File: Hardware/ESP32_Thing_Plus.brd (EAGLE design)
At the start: 22.9 x 58.4 mm, 106 parts, among them J3 QWIIC_RIGHT_ANGLE, J6 microSD, Q2 MBT3904DW1T1, Q3 20V/4.2A/52mΩ/1.4W, U1 MCP73831, U2 ESP-WROOM-32NARROW, U3 AP2112K-3.3, U4 MAX17048, U5 AP2112K-3.3, U6 THINGPLUS_LOGICAL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

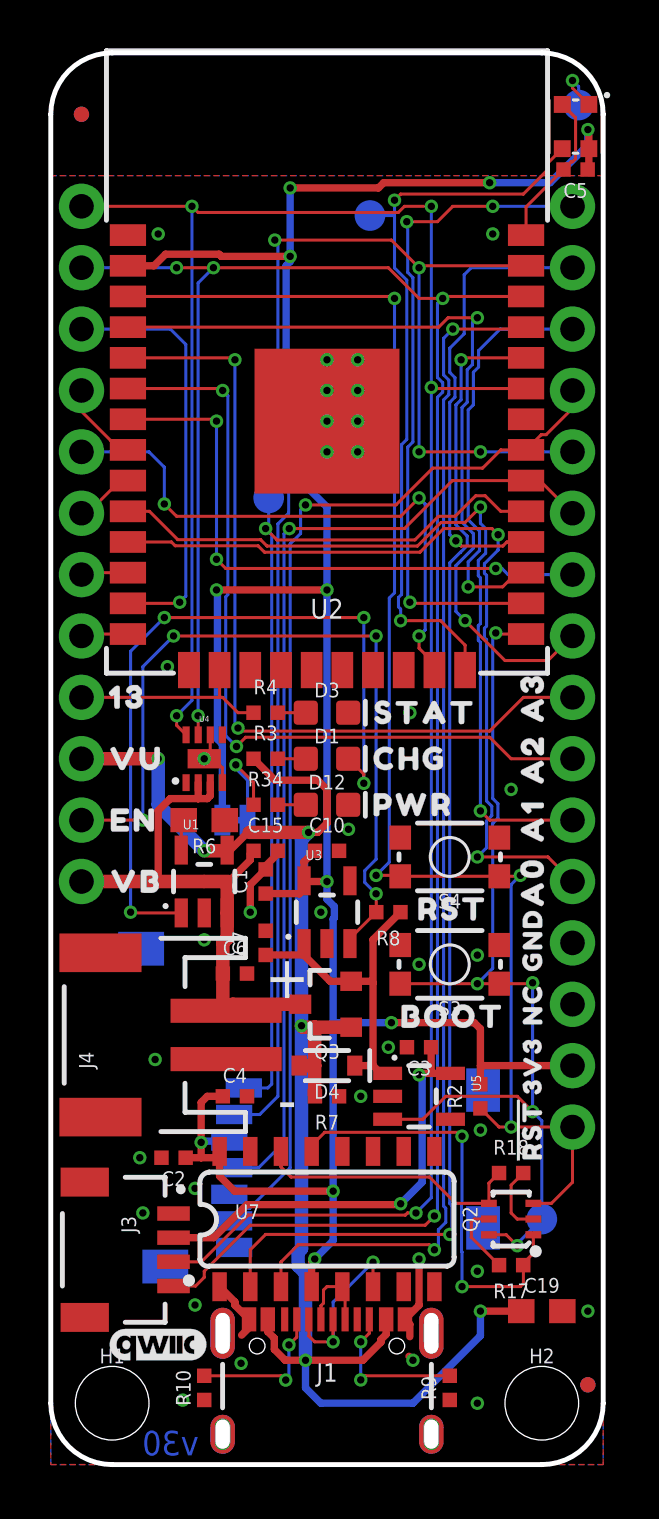
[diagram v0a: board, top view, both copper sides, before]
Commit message: Add test sketches
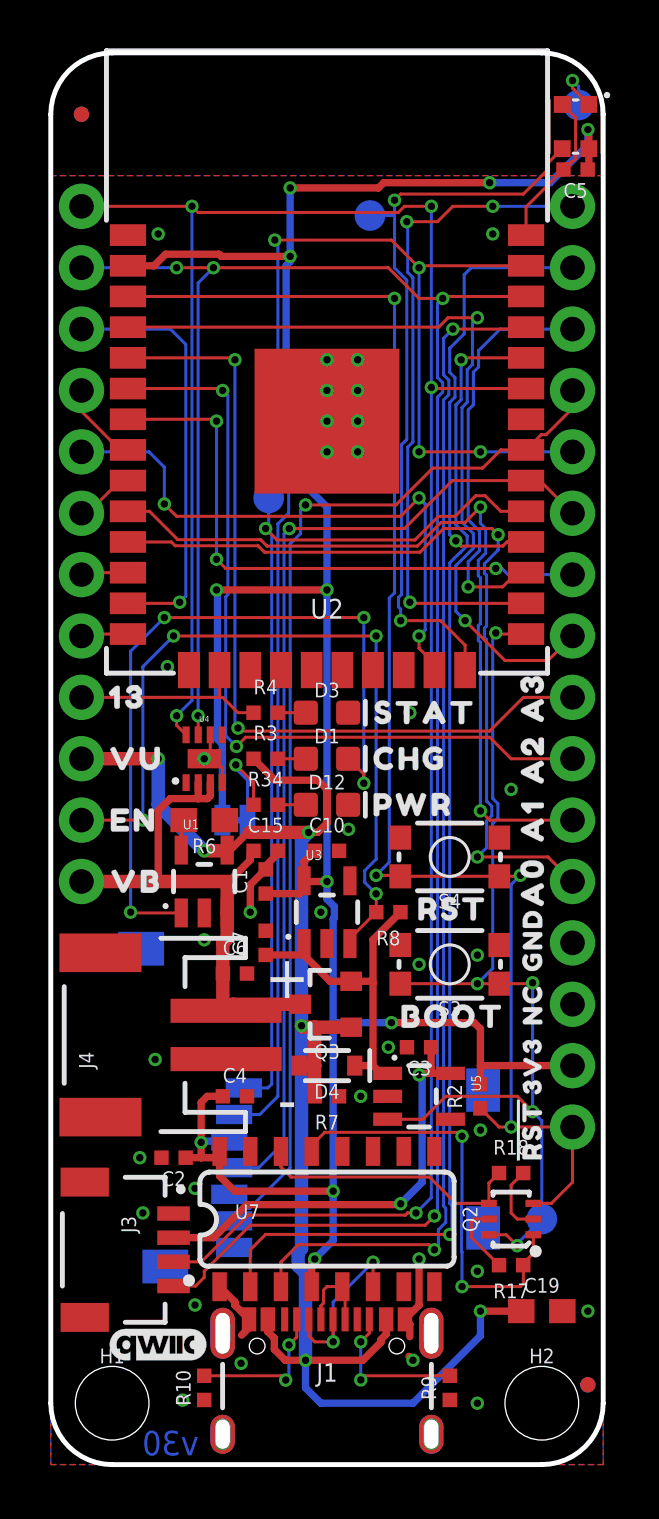
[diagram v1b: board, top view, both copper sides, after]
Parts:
- moved U$59 71.2 mm to (100.3, 53.3)
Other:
- board text removed: "Mike Hord"
- board text removed: "Revised by: Alex Wende"
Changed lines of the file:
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@@
 <layer number="47" name="Measures" color="7" fill="1" visible="no" active="yes"/>
 <layer number="48" name="Document" color="7" fill="1" visible="no" active="yes"/>
-<layer number="49" name="Reference" color="7" fill="1" visible="yes" active="yes"/>
+<layer number="49" name="Reference" color="7" fill="1" visible="no" active="yes"/>
 <layer number="50" name="dxf" color="7" fill="1" visible="no" active="yes"/>
 <layer number="51" name="tDocu" color="6" fill="1" visible="yes" active="yes"/>
@@
 <board>
 <plain>
-<text x="13.97" y="-19.05" size="1.778" layer="51" font="vector" ratio="15">Mike Hord</text>
 <wire x1="22.86" y1="2.54" x2="22.86" y2="55.88" width="0.2032" layer="20"/>
 <wire x1="22.86" y1="55.88" x2="20.32" y2="58.42" width="0.2032" layer="20" curve="90"/>
@@
 <dimension x1="22.86" y1="2.54" x2="0" y2="2.54" x3="11.43" y3="-8.89" textsize="1.778" layer="47" unit="inch"/>
 <dimension x1="2.54" y1="0" x2="2.54" y2="58.42" x3="-16.51" y3="29.21" textsize="1.778" layer="47" unit="inch"/>
-<text x="-5.08" y="-21.59" size="1.778" layer="51" font="vector">Revised by: Alex Wende</text>
 <text x="9.779" y="20.193" size="1.778" layer="21" font="vector" ratio="15" align="center">+</text>
 <text x="9.779" y="15.113" size="1.778" layer="21" font="vector" ratio="15" align="center">-</text>
@@
 <attribute name="VALUE" value="10k" x="13.97" y="23.622" size="0.6096" layer="27" font="vector" ratio="20" rot="R180" align="top-center"/>
 </element>
-<element name="U$59" library="SparkFun-Aesthetics" package="ORDERING_INSTRUCTIONS" value="" x="29.21" y="50.8" smashed="yes"/>
+<element name="U$59" library="SparkFun-Aesthetics" package="ORDERING_INSTRUCTIONS" value="" x="100.33" y="53.34" smashed="yes"/>
 <element name="FD1" library="SparkFun-Aesthetics" package="FIDUCIAL-MICRO" value="FIDUCIALUFIDUCIAL" x="1.27" y="55.88" smashed="yes"/>
 <element name="FD2" library="SparkFun-Aesthetics" package="FIDUCIAL-MICRO" value="FIDUCIALUFIDUCIAL" x="1.27" y="55.88" smashed="yes" rot="MR0"/>
@@
 <contactref element="C15" pad="1"/>
 <wire x1="1.27" y1="24.13" x2="4.445" y2="24.13" width="0.5588" layer="1"/>
-<wire x1="4.445" y1="24.13" x2="6.35" y2="24.13" width="0.5588" layer="1"/>
-<wire x1="6.35" y1="24.13" x2="7.366" y2="24.13" width="0.5588" layer="1"/>
+<wire x1="4.445" y1="24.13" x2="7.366" y2="24.13" width="0.5588" layer="1"/>
 <wire x1="8.255" y1="25.265" x2="8.39" y2="25.4" width="0.3048" layer="1"/>
 <wire x1="7.366" y1="24.13" x2="8.255" y2="25.019" width="0.3048" layer="1"/>
@@
 <wire x1="14.097" y1="50.673" x2="9.271" y2="50.673" width="0.127" layer="1"/>
 <via x="9.271" y="50.673" extent="1-16" drill="0.3048"/>
-<wire x1="9.271" y1="50.673" x2="9.3345" y2="50.6095" width="0.127" layer="16"/>
 <wire x1="15.24" y1="49.53" x2="14.097" y2="50.673" width="0.127" layer="1"/>
 <wire x1="9.398" y1="15.24" x2="9.398" y2="38.92964375" width="0.127" layer="16"/>
 <wire x1="9.8425" y1="39.37414375" x2="9.8425" y2="40.7265625" width="0.127" layer="16"/>
 <wire x1="9.8425" y1="40.7265625" x2="9.398" y2="41.1710625" width="0.127" layer="16"/>
-<wire x1="9.398" y1="50.546" x2="9.3345" y2="50.6095" width="0.127" layer="16"/>
+<wire x1="9.398" y1="50.546" x2="9.271" y2="50.673" width="0.127" layer="16"/>
 <wire x1="9.398" y1="38.92964375" x2="9.8425" y2="39.37414375" width="0.127" layer="16"/>
 <wire x1="9.398" y1="41.1710625" x2="9.398" y2="50.546" width="0.127" layer="16"/>
